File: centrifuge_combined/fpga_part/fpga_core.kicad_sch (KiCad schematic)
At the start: 14 parts, among them U1 XC7A100T-FTG256

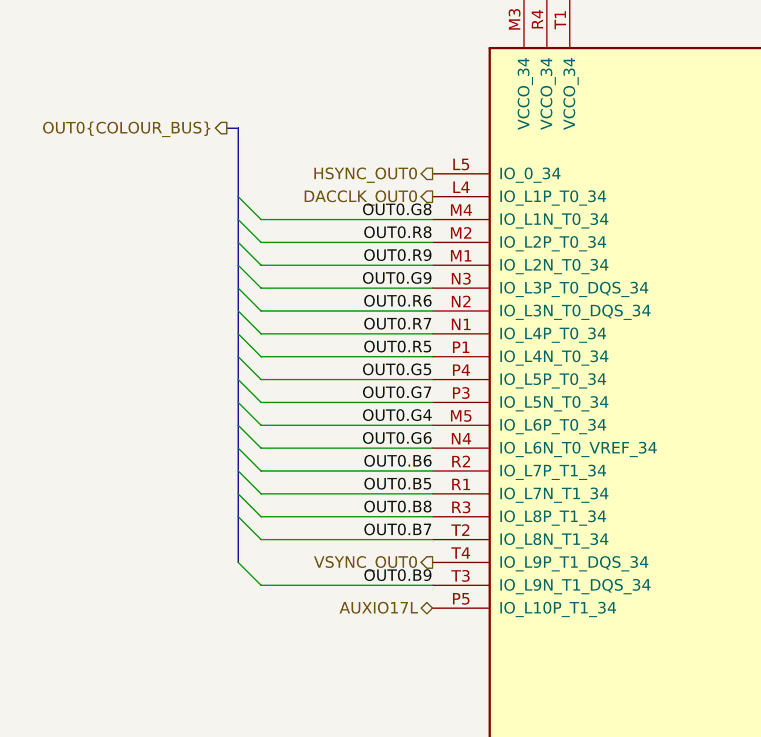
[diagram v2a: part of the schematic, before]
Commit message: fix mismatch between VSYNC and HSYNC out, only needs a swap in constraints file as well
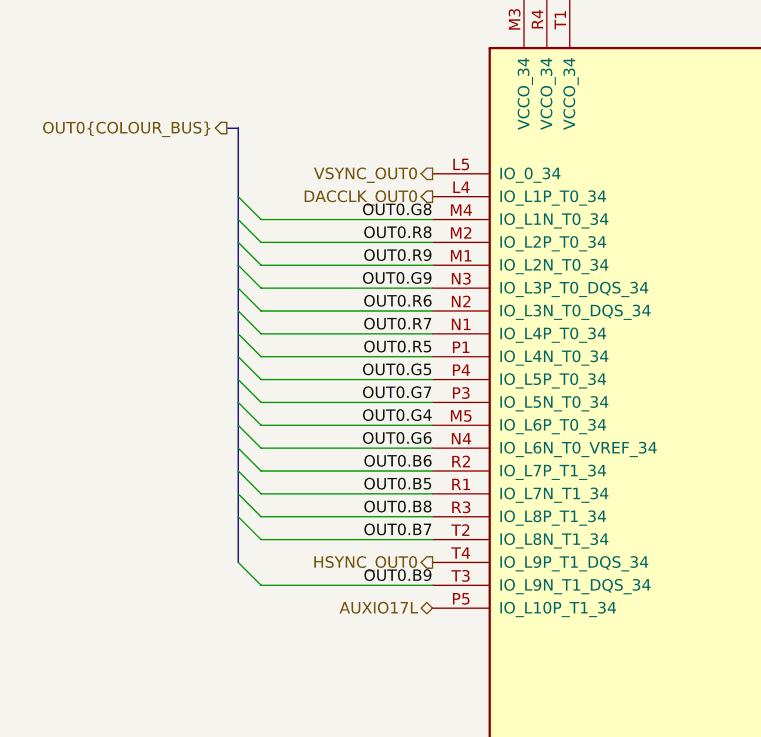
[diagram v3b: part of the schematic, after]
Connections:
- net HSYNC_OUT0: now also U1.T4 (IO_L9P_T1_DQS_34); no longer U1.L5 (IO_0_34)
- net VSYNC_OUT0: now also U1.L5 (IO_0_34); no longer U1.T4 (IO_L9P_T1_DQS_34)
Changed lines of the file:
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@@
     (effects (font (size 1.27 1.27)) (justify left))
   )
-  (hierarchical_label "VSYNC_OUT0" (shape output) (at 56.388 86.741 180)
+  (hierarchical_label "HSYNC_OUT0" (shape output) (at 56.388 86.741 180)
     (effects (font (size 1.27 1.27)) (justify right))
   )
@@
     (effects (font (size 1.27 1.27)) (justify right))
   )
-  (hierarchical_label "HSYNC_OUT0" (shape output) (at 56.388 43.561 180)
+  (hierarchical_label "VSYNC_OUT0" (shape output) (at 56.388 43.561 180)
     (effects (font (size 1.27 1.27)) (justify right))
   )

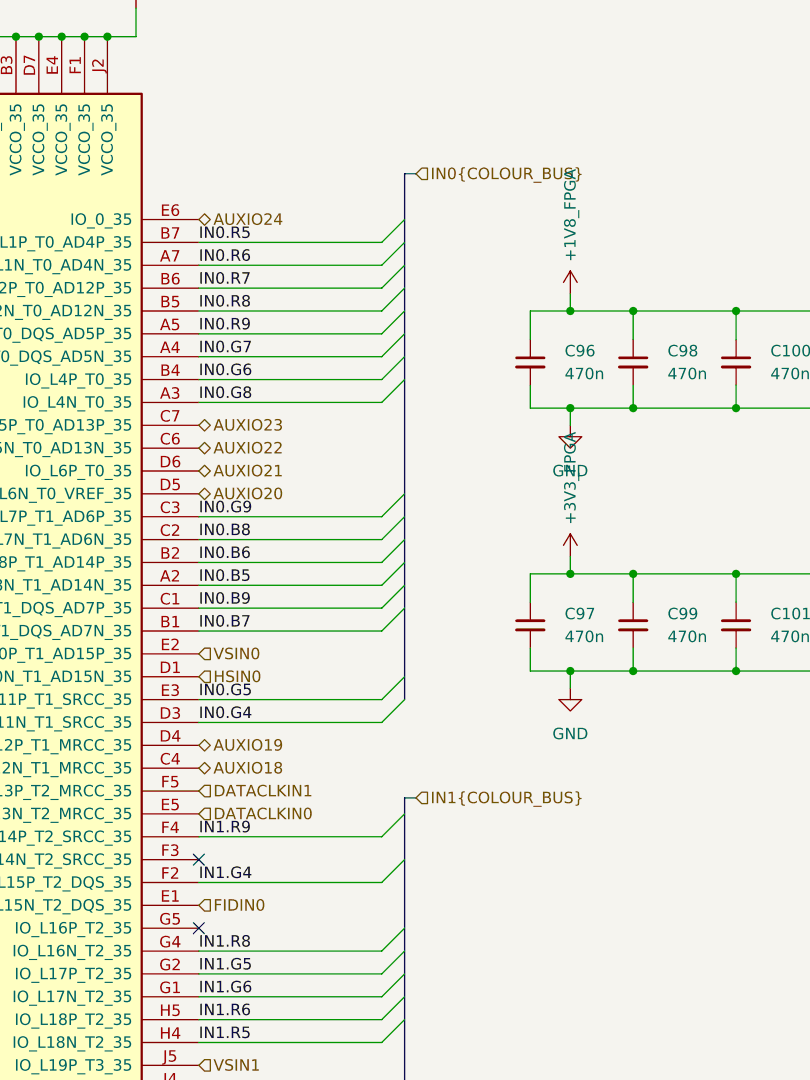
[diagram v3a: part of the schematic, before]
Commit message: fully commit to calling top VGA ADC2
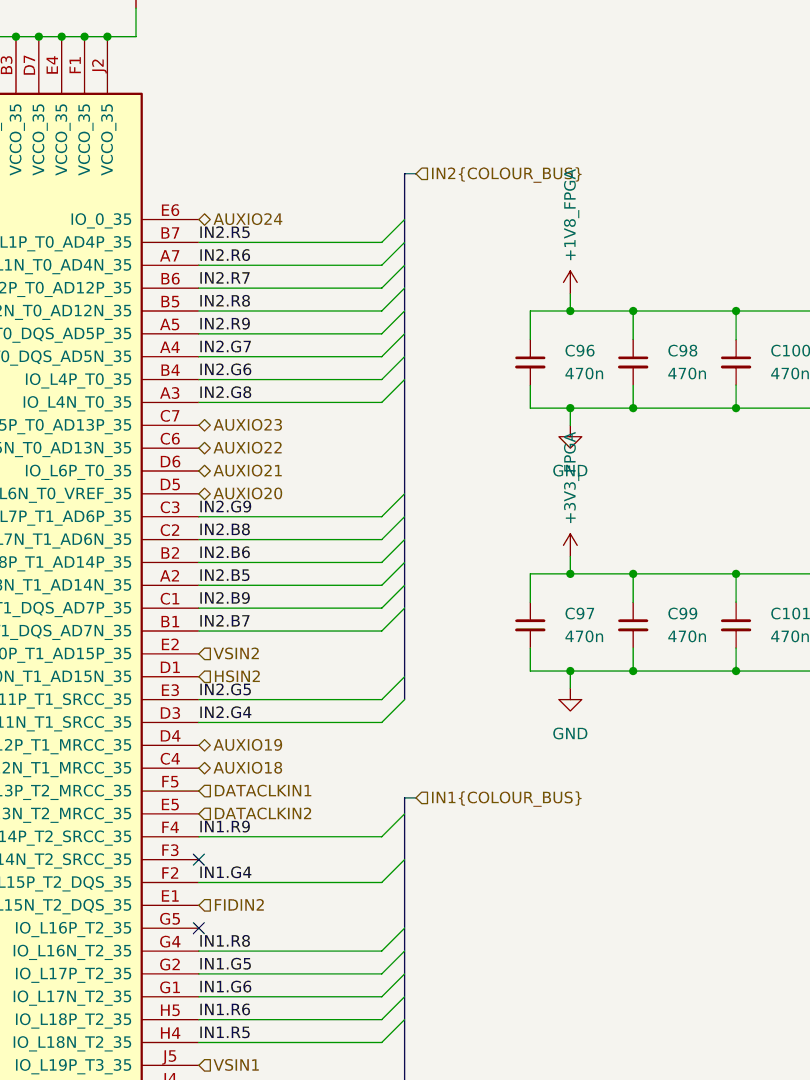
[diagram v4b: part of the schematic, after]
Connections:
- net DATACLKIN0 renamed DATACLKIN2
- net FIDIN0 renamed FIDIN2
- net HSIN0 renamed HSIN2
- net IN0.B5 renamed IN2.B5
- net IN0.B6 renamed IN2.B6
- net IN0.B7 renamed IN2.B7
- net IN0.B8 renamed IN2.B8
- net IN0.B9 renamed IN2.B9
- net IN0.G4 renamed IN2.G4
- net IN0.G5 renamed IN2.G5
- net IN0.G6 renamed IN2.G6
- net IN0.G7 renamed IN2.G7
- net IN0.G8 renamed IN2.G8
- net IN0.G9 renamed IN2.G9
- net IN0.R5 renamed IN2.R5
- net IN0.R6 renamed IN2.R6
- net IN0.R7 renamed IN2.R7
- net IN0.R8 renamed IN2.R8
- net IN0.R9 renamed IN2.R9
- net VSIN0 renamed VSIN2
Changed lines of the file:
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@@
     (stroke (width 0) (type default) (color 0 0 0 0))
   )
-  (label "IN0.R5" (at 157.988 46.101 0)
-    (effects (font (size 1.27 1.27)) (justify left bottom))
-  )
-  (label "IN0.B7" (at 157.988 89.281 0)
+  (label "IN2.R5" (at 157.988 46.101 0)
+    (effects (font (size 1.27 1.27)) (justify left bottom))
+  )
+  (label "IN2.B7" (at 157.988 89.281 0)
     (effects (font (size 1.27 1.27)) (justify left bottom))
   )
@@
     (effects (font (size 1.27 1.27)) (justify left bottom))
   )
-  (label "IN0.B5" (at 157.988 84.201 0)
+  (label "IN2.B5" (at 157.988 84.201 0)
     (effects (font (size 1.27 1.27)) (justify left bottom))
   )
@@
     (effects (font (size 1.27 1.27)) (justify left bottom))
   )
-  (label "IN0.G4" (at 157.988 99.441 0)
+  (label "IN2.G4" (at 157.988 99.441 0)
     (effects (font (size 1.27 1.27)) (justify left bottom))
   )
@@
     (effects (font (size 1.27 1.27)) (justify right bottom))
   )
-  (label "IN0.B6" (at 157.988 81.661 0)
+  (label "IN2.B6" (at 157.988 81.661 0)
     (effects (font (size 1.27 1.27)) (justify left bottom))
   )
@@
     (effects (font (size 1.27 1.27)) (justify left bottom))
   )
-  (label "IN0.R9" (at 157.988 56.261 0)
-    (effects (font (size 1.27 1.27)) (justify left bottom))
-  )
-  (label "IN0.G9" (at 157.988 76.581 0)
+  (label "IN2.R9" (at 157.988 56.261 0)
+    (effects (font (size 1.27 1.27)) (justify left bottom))
+  )
+  (label "IN2.G9" (at 157.988 76.581 0)
     (effects (font (size 1.27 1.27)) (justify left bottom))
   )
@@
     (effects (font (size 1.27 1.27)) (justify left bottom))
   )
-  (label "IN0.R8" (at 157.988 53.721 0)
-    (effects (font (size 1.27 1.27)) (justify left bottom))
-  )
-  (label "IN0.B9" (at 157.988 86.741 0)
+  (label "IN2.R8" (at 157.988 53.721 0)
+    (effects (font (size 1.27 1.27)) (justify left bottom))
+  )
+  (label "IN2.B9" (at 157.988 86.741 0)
     (effects (font (size 1.27 1.27)) (justify left bottom))
   )
@@
     (effects (font (size 1.27 1.27)) (justify right bottom))
   )
-  (label "IN0.G7" (at 157.988 58.801 0)
+  (label "IN2.G7" (at 157.988 58.801 0)
     (effects (font (size 1.27 1.27)) (justify left bottom))
   )
@@
     (effects (font (size 1.27 1.27)) (justify right bottom))
   )
-  (label "IN0.R7" (at 157.988 51.181 0)
-    (effects (font (size 1.27 1.27)) (justify left bottom))
-  )
-  (label "IN0.R6" (at 157.988 48.641 0)
+  (label "IN2.R7" (at 157.988 51.181 0)
+    (effects (font (size 1.27 1.27)) (justify left bottom))
+  )
+  (label "IN2.R6" (at 157.988 48.641 0)
     (effects (font (size 1.27 1.27)) (justify left bottom))
   )
@@
     (effects (font (size 1.27 1.27)) (justify right bottom))
   )
-  (label "IN0.B8" (at 157.988 79.121 0)
+  (label "IN2.B8" (at 157.988 79.121 0)
     (effects (font (size 1.27 1.27)) (justify left bottom))
   )
@@
     (effects (font (size 1.27 1.27)) (justify right bottom))
   )
-  (label "IN0.G5" (at 157.988 96.901 0)
+  (label "IN2.G5" (at 157.988 96.901 0)
     (effects (font (size 1.27 1.27)) (justify left bottom))
   )
@@
     (effects (font (size 1.27 1.27)) (justify right bottom))
   )
-  (label "IN0.G8" (at 157.988 63.881 0)
-    (effects (font (size 1.27 1.27)) (justify left bottom))
-  )
-  (label "IN0.G6" (at 157.988 61.341 0)
+  (label "IN2.G8" (at 157.988 63.881 0)
+    (effects (font (size 1.27 1.27)) (justify left bottom))
+  )
+  (label "IN2.G6" (at 157.988 61.341 0)
     (effects (font (size 1.27 1.27)) (justify left bottom))
   )
@@
     (effects (font (size 1.27 1.27)) (justify left))
   )
-  (hierarchical_label "HSIN0" (shape input) (at 157.988 94.361 0)
+  (hierarchical_label "HSIN2" (shape input) (at 157.988 94.361 0)
     (effects (font (size 1.27 1.27)) (justify left))
   )
@@
     (effects (font (size 1.27 1.27)) (justify left))
   )
-  (hierarchical_label "IN0{COLOUR_BUS}" (shape input) (at 182.118 38.481 0)
+  (hierarchical_label "IN2{COLOUR_BUS}" (shape input) (at 182.118 38.481 0)
     (effects (font (size 1.27 1.27)) (justify left))
   )
@@
     (effects (font (size 1.27 1.27)) (justify left))
   )
-  (hierarchical_label "VSIN0" (shape input) (at 157.988 91.821 0)
-    (effects (font (size 1.27 1.27)) (justify left))
-  )
-  (hierarchical_label "DATACLKIN0" (shape input) (at 157.988 109.601 0)
+  (hierarchical_label "VSIN2" (shape input) (at 157.988 91.821 0)
+    (effects (font (size 1.27 1.27)) (justify left))
+  )
+  (hierarchical_label "DATACLKIN2" (shape input) (at 157.988 109.601 0)
     (effects (font (size 1.27 1.27)) (justify left))
   )
@@
     (effects (font (size 1.27 1.27)) (justify left))
   )
-  (hierarchical_label "FIDIN0" (shape input) (at 157.988 119.761 0)
-    (effects (font (size 1.27 1.27)) (justify left))
-  )
+  (hierarchical_label "FIDIN2" (shape input) (at 157.988 119.761 0)
+    (effects (font (size 1.27 1.27)) (justify left))
+  )
